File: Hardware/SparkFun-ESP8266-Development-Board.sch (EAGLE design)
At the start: 69 parts, among them J1 U.FL, Q1 2.5A/30V, Q2 MMBT2222A, U1 ESP8266, U2 MCP73831, U3 AT25SF041-SOIC8, U4 AP2112K-3.3V, U5 ATECC108-SSHDA, Y1 26MHz

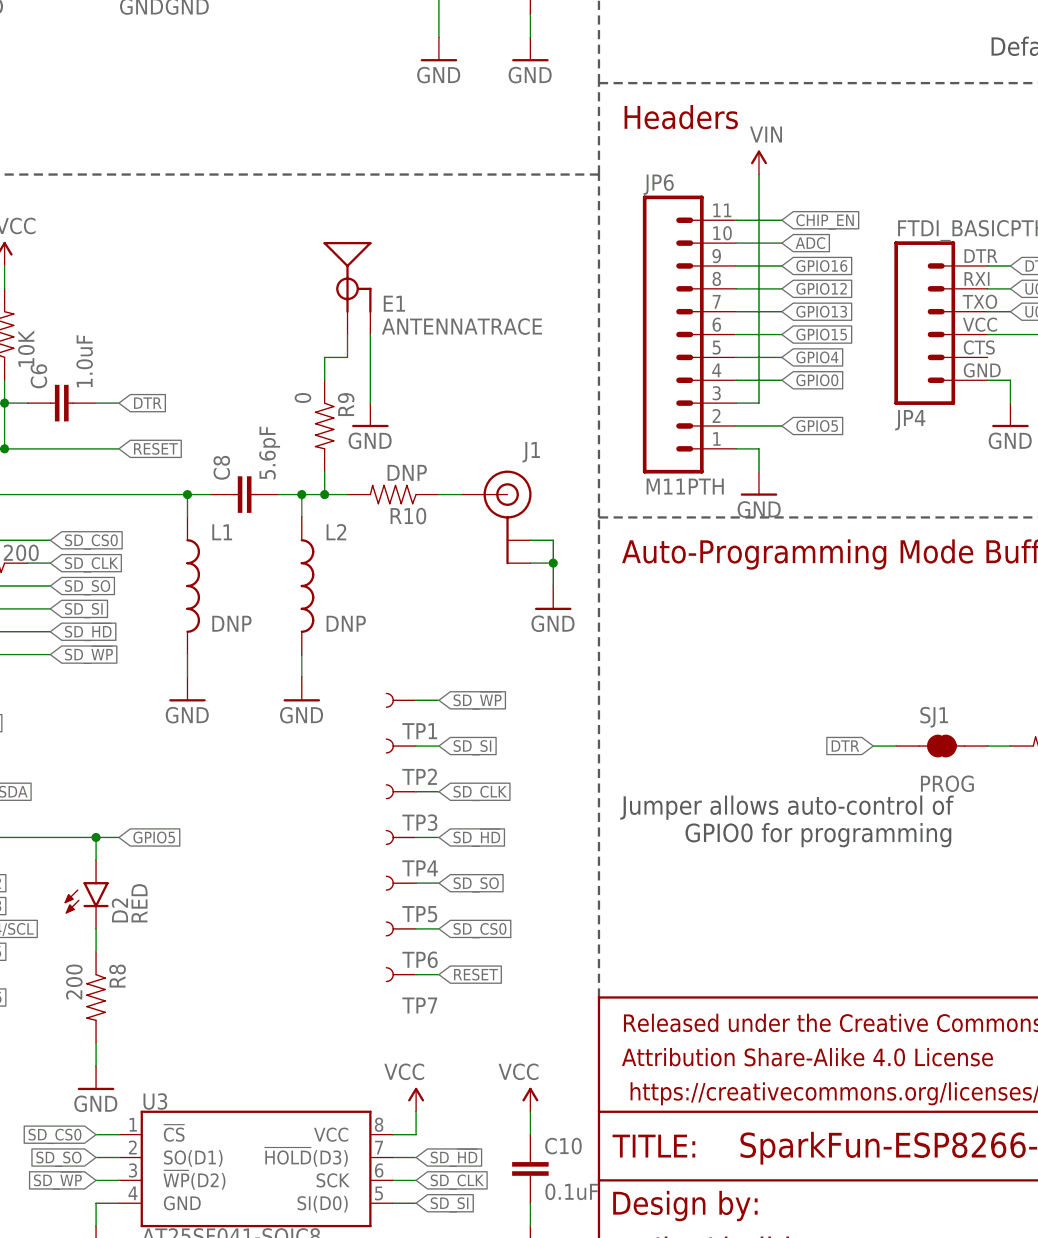
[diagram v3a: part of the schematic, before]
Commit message: Adding pull-down resistor to GPIO15 (required to upload). Not broken out any more.
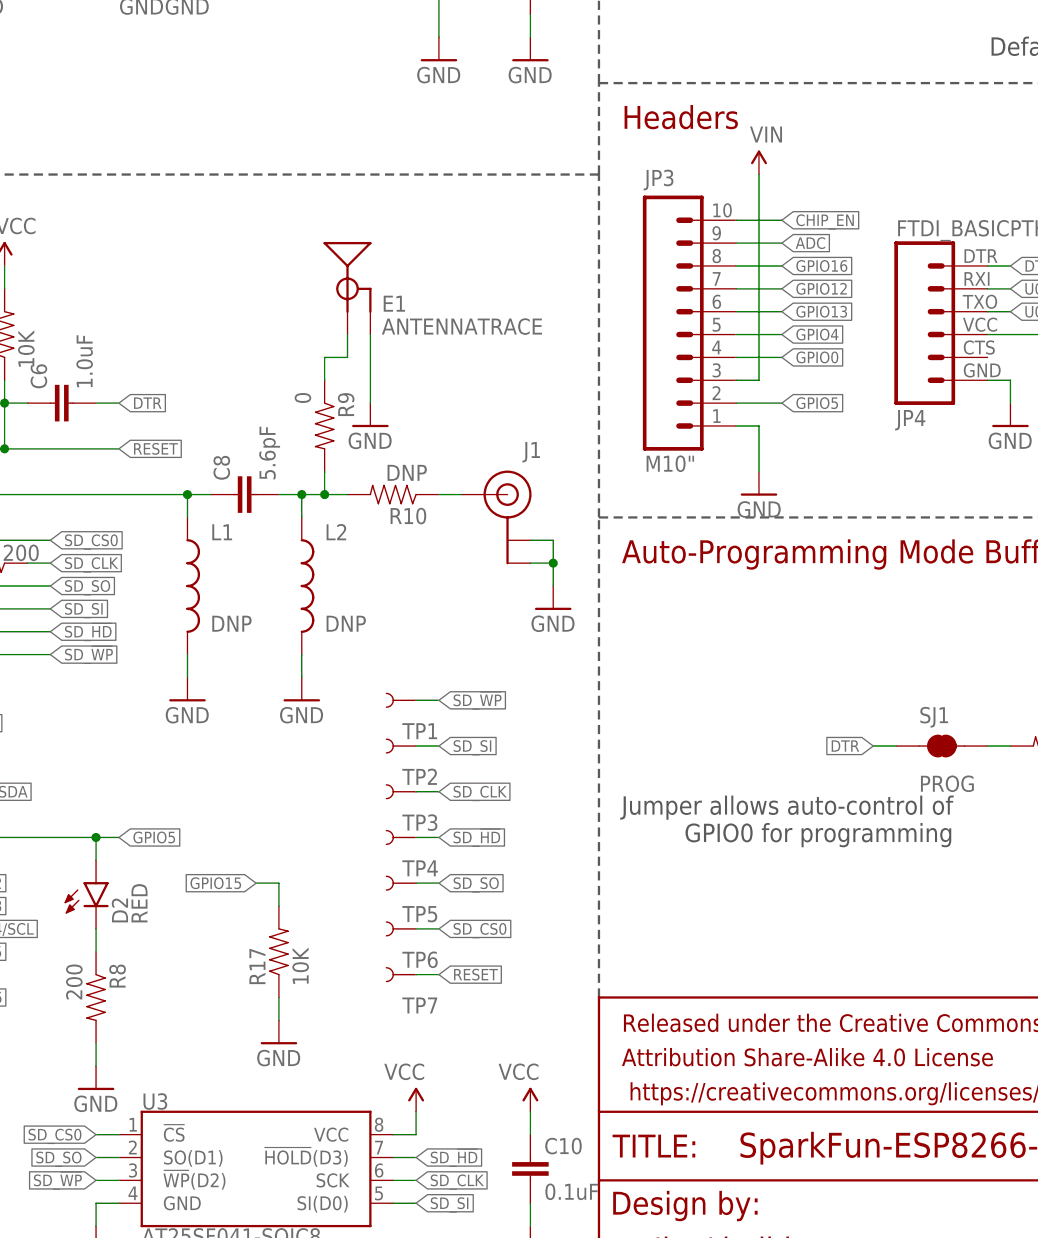
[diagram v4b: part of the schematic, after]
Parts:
- removed JP6: M11PTH, SparkFun-Connectors:M11PTH
- added JP3: M10", SparkFun-Connectors:M10"
- added R17: 10K, SparkFun-Resistors:10KOHM1/10W1%(0603)0603
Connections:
- net ADC: now also JP3.9; no longer JP6.10
- net CHIP_EN: now also JP3.10; no longer JP6.11
- net GND: now also JP3.1, R17.1; no longer JP6.1
- net GPIO0: now also JP3.4; no longer JP6.4
- net GPIO12: now also JP3.7; no longer JP6.8
- net GPIO13: now also JP3.6; no longer JP6.7
- net GPIO15: now also R17.2; no longer JP6.6
- net GPIO16: now also JP3.8; no longer JP6.9
- net GPIO4: now also JP3.5; no longer JP6.5
- net GPIO5: now also JP3.2; no longer JP6.2
- net VIN: now also JP3.3; no longer JP6.3
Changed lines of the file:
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@@
 <part name="R16" library="SparkFun-Resistors" deviceset="200OHM1/10W1%(0603)" device="" value="200"/>
 <part name="GND27" library="SparkFun-Aesthetics" deviceset="GND" device=""/>
-<part name="JP6" library="SparkFun-Connectors" deviceset="M11" device="PTH"/>
+<part name="JP3" library="SparkFun-Connectors" deviceset="M10" device="&quot;"/>
+<part name="R17" library="SparkFun-Resistors" deviceset="10KOHM1/10W1%(0603)" device="0603" value="10K"/>
+<part name="GND28" library="SparkFun-Aesthetics" deviceset="GND" device=""/>
 </parts>
 <sheets>
@@
 <instance part="R16" gate="G$1" x="139.7" y="149.86" rot="R270"/>
 <instance part="GND27" gate="1" x="139.7" y="139.7"/>
-<instance part="JP6" gate="G$1" x="152.4" y="109.22"/>
+<instance part="JP3" gate="G$1" x="152.4" y="116.84"/>
+<instance part="R17" gate="G$1" x="111.76" y="40.64" rot="R90"/>
+<instance part="GND28" gate="1" x="111.76" y="30.48"/>
 </instances>
 <busses>
@@
 </segment>
 <segment>
-<wire x1="165.1" y1="96.52" x2="165.1" y2="93.98" width="0.1524" layer="91"/>
 <pinref part="GND22" gate="1" pin="GND"/>
-<pinref part="JP6" gate="G$1" pin="1"/>
-<wire x1="162.56" y1="96.52" x2="165.1" y2="96.52" width="0.1524" layer="91"/>
+<pinref part="JP3" gate="G$1" pin="1"/>
+<wire x1="162.56" y1="99.06" x2="165.1" y2="99.06" width="0.1524" layer="91"/>
+<wire x1="165.1" y1="99.06" x2="165.1" y2="93.98" width="0.1524" layer="91"/>
 </segment>
 <segment>
@@
 <pinref part="GND27" gate="1" pin="GND"/>
 <wire x1="139.7" y1="142.24" x2="139.7" y2="144.78" width="0.1524" layer="91"/>
+</segment>
+<segment>
+<pinref part="R17" gate="G$1" pin="1"/>
+<pinref part="GND28" gate="1" pin="GND"/>
+<wire x1="111.76" y1="33.02" x2="111.76" y2="35.56" width="0.1524" layer="91"/>
 </segment>
 </net>
@@
 <wire x1="162.56" y1="121.92" x2="167.64" y2="121.92" width="0.1524" layer="91"/>
 <label x="167.64" y="121.92" size="1.27" layer="95" xref="yes"/>
-<pinref part="JP6" gate="G$1" pin="11"/>
+<pinref part="JP3" gate="G$1" pin="10"/>
 </segment>
 </net>
@@
 <wire x1="162.56" y1="119.38" x2="167.64" y2="119.38" width="0.1524" layer="91"/>
 <label x="167.64" y="119.38" size="1.27" layer="95" xref="yes"/>
-<pinref part="JP6" gate="G$1" pin="10"/>
+<pinref part="JP3" gate="G$1" pin="9"/>
 </segment>
 </net>
@@
 </segment>
 <segment>
-<wire x1="162.56" y1="104.14" x2="167.64" y2="104.14" width="0.1524" layer="91"/>
-<label x="167.64" y="104.14" size="1.27" layer="95" xref="yes"/>
-<pinref part="JP6" gate="G$1" pin="4"/>
+<wire x1="162.56" y1="106.68" x2="167.64" y2="106.68" width="0.1524" layer="91"/>
+<label x="167.64" y="106.68" size="1.27" layer="95" xref="yes"/>
+<pinref part="JP3" gate="G$1" pin="4"/>
 </segment>
 </net>
@@
 </segment>
 <segment>
-<pinref part="JP6" gate="G$1" pin="2"/>
-<wire x1="162.56" y1="99.06" x2="167.64" y2="99.06" width="0.1524" layer="91"/>
-<label x="167.64" y="99.06" size="1.27" layer="95" xref="yes"/>
+<pinref part="JP3" gate="G$1" pin="2"/>
+<wire x1="162.56" y1="101.6" x2="167.64" y2="101.6" width="0.1524" layer="91"/>
+<label x="167.64" y="101.6" size="1.27" layer="95" xref="yes"/>
 </segment>
 </net>
@@
 </segment>
 <segment>
-<wire x1="162.56" y1="106.68" x2="167.64" y2="106.68" width="0.1524" layer="91"/>
-<label x="167.64" y="106.68" size="1.27" layer="95" xref="yes"/>
-<pinref part="JP6" gate="G$1" pin="5"/>
+<pinref part="JP3" gate="G$1" pin="5"/>
+<wire x1="162.56" y1="109.22" x2="167.64" y2="109.22" width="0.1524" layer="91"/>
+<label x="167.64" y="109.22" size="1.27" layer="95" xref="yes"/>
 </segment>
 </net>
@@
 <wire x1="162.56" y1="116.84" x2="167.64" y2="116.84" width="0.1524" layer="91"/>
 <label x="167.64" y="116.84" size="1.27" layer="95" xref="yes"/>
-<pinref part="JP6" gate="G$1" pin="9"/>
+<pinref part="JP3" gate="G$1" pin="8"/>
 </segment>
 </net>
@@
 </segment>
 <segment>
-<wire x1="162.56" y1="109.22" x2="167.64" y2="109.22" width="0.1524" layer="91"/>
-<label x="167.64" y="109.22" size="1.27" layer="95" xref="yes"/>
-<pinref part="JP6" gate="G$1" pin="6"/>
+<pinref part="R17" gate="G$1" pin="2"/>
+<wire x1="111.76" y1="45.72" x2="111.76" y2="48.26" width="0.1524" layer="91"/>
+<wire x1="111.76" y1="48.26" x2="109.22" y2="48.26" width="0.1524" layer="91"/>
+<label x="109.22" y="48.26" size="1.27" layer="95" rot="R180" xref="yes"/>
 </segment>
 </net>
@@
 <wire x1="162.56" y1="111.76" x2="167.64" y2="111.76" width="0.1524" layer="91"/>
 <label x="167.64" y="111.76" size="1.27" layer="95" xref="yes"/>
-<pinref part="JP6" gate="G$1" pin="7"/>
+<pinref part="JP3" gate="G$1" pin="6"/>
 </segment>
 </net>
@@
 <wire x1="162.56" y1="114.3" x2="167.64" y2="114.3" width="0.1524" layer="91"/>
 <label x="167.64" y="114.3" size="1.27" layer="95" xref="yes"/>
-<pinref part="JP6" gate="G$1" pin="8"/>
+<pinref part="JP3" gate="G$1" pin="7"/>
 </segment>
 </net>
@@
 </segment>
 <segment>
-<wire x1="162.56" y1="101.6" x2="165.1" y2="101.6" width="0.1524" layer="91"/>
-<wire x1="165.1" y1="101.6" x2="165.1" y2="127" width="0.1524" layer="91"/>
 <pinref part="SUPPLY8" gate="G$1" pin="VIN"/>
-<pinref part="JP6" gate="G$1" pin="3"/>
-</segment>
-</net>
+<pinref part="JP3" gate="G$1" pin="3"/>
+<wire x1="165.1" y1="104.14" x2="165.1" y2="127" width="0.1524" layer="91"/>
+<wire x1="162.56" y1="104.14" x2="165.1" y2="104.14" width="0.1524" layer="91"/>
+</segment>
+</net>

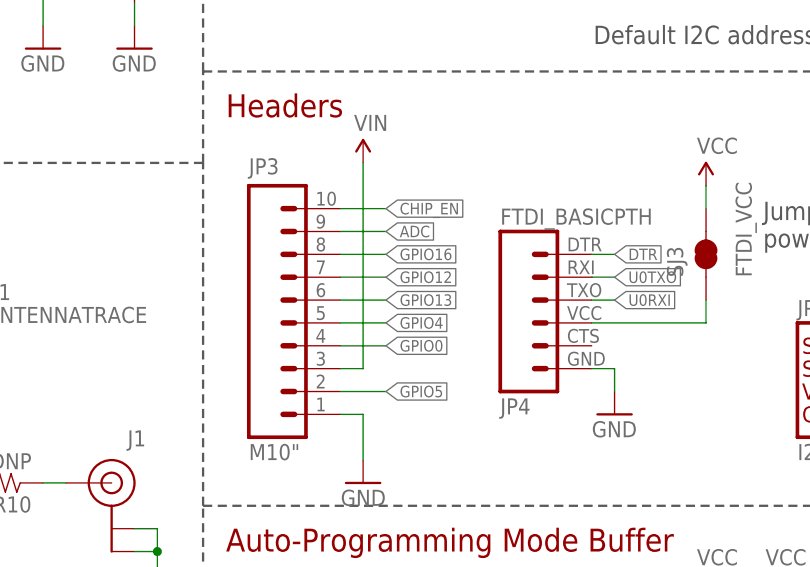
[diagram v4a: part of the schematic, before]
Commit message: Re-arranging 10-pin header pin-out.
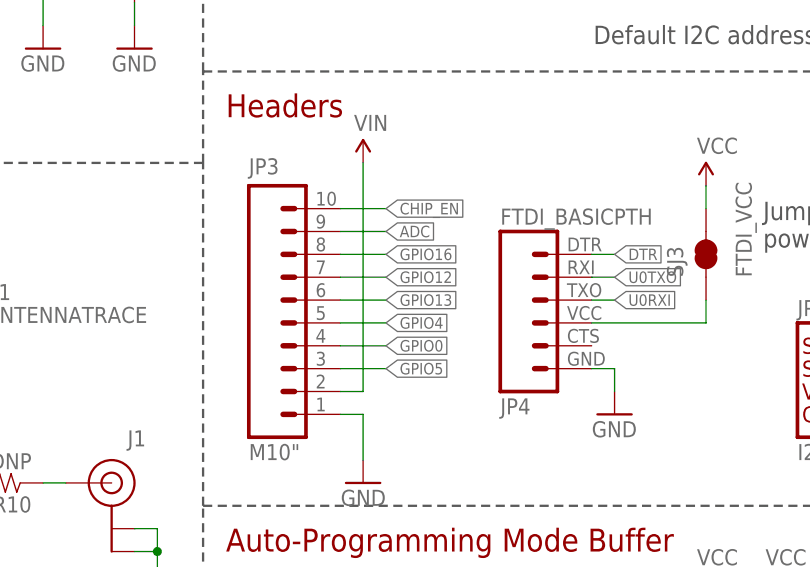
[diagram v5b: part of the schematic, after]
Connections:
- net GPIO5: now also JP3.3; no longer JP3.2
- net VIN: now also JP3.2; no longer JP3.3
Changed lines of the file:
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@@
 </segment>
 <segment>
-<pinref part="JP3" gate="G$1" pin="2"/>
-<wire x1="162.56" y1="101.6" x2="167.64" y2="101.6" width="0.1524" layer="91"/>
-<label x="167.64" y="101.6" size="1.27" layer="95" xref="yes"/>
+<pinref part="JP3" gate="G$1" pin="3"/>
+<wire x1="162.56" y1="104.14" x2="167.64" y2="104.14" width="0.1524" layer="91"/>
+<label x="167.64" y="104.14" size="1.27" layer="95" xref="yes"/>
 </segment>
 </net>
@@
 <segment>
 <pinref part="SUPPLY8" gate="G$1" pin="VIN"/>
-<pinref part="JP3" gate="G$1" pin="3"/>
-<wire x1="165.1" y1="104.14" x2="165.1" y2="127" width="0.1524" layer="91"/>
-<wire x1="162.56" y1="104.14" x2="165.1" y2="104.14" width="0.1524" layer="91"/>
-</segment>
-</net>
+<wire x1="165.1" y1="101.6" x2="165.1" y2="127" width="0.1524" layer="91"/>
+<pinref part="JP3" gate="G$1" pin="2"/>
+<wire x1="162.56" y1="101.6" x2="165.1" y2="101.6" width="0.1524" layer="91"/>
+</segment>
+</net>
